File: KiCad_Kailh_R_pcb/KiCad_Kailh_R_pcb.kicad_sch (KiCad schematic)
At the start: 66 parts, among them J1 AudioJack3_SwitchTR, J2 Reset, SW1 Esc, SW10 E, SW11 R, SW12 T, SW13 Ctrl, SW14 A, SW15 S, SW16 D, SW17 F, SW18 G, SW19 Shift, SW2 1, SW20 Z, SW21 X, SW22 C, SW23 V, SW24 6, SW25 Fn, SW26 Alt, SW27 Win, SW28 NoConv, SW29 Space, SW3 2, SW4 3, SW5 4, SW6 5, SW7 Tab, SW8 Q, SW9 W, U1 Sparkfun_Pro_Micro

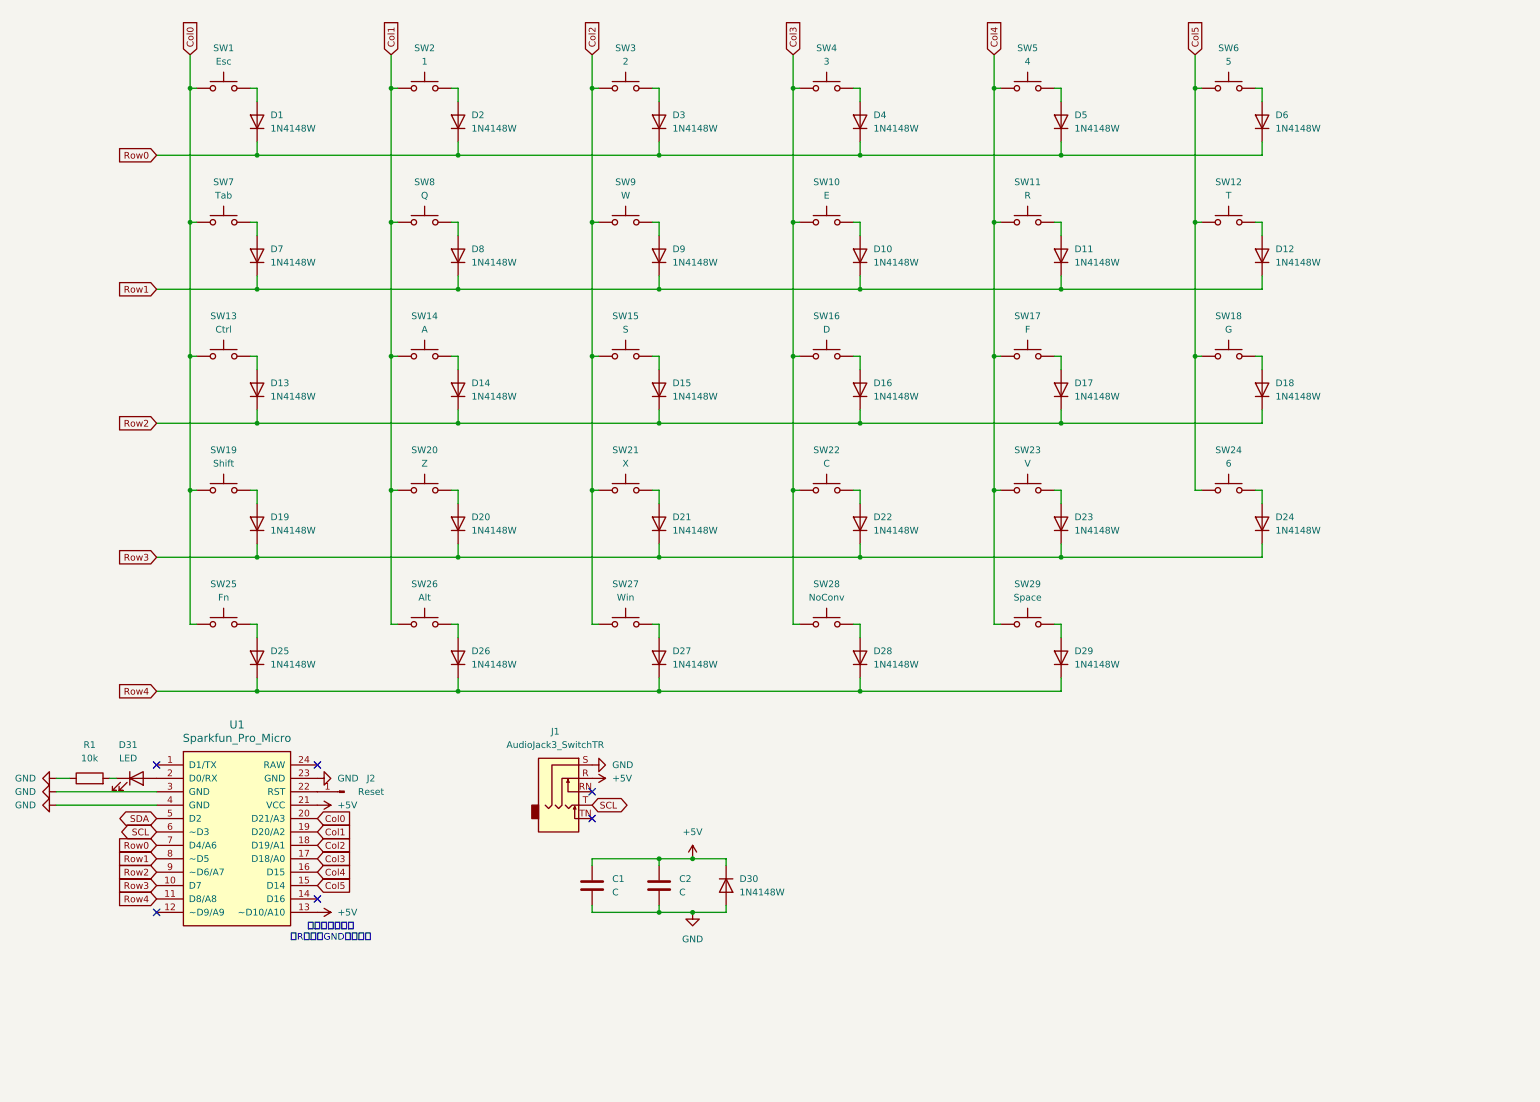
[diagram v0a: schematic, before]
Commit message: feat: Rightのガワを用意
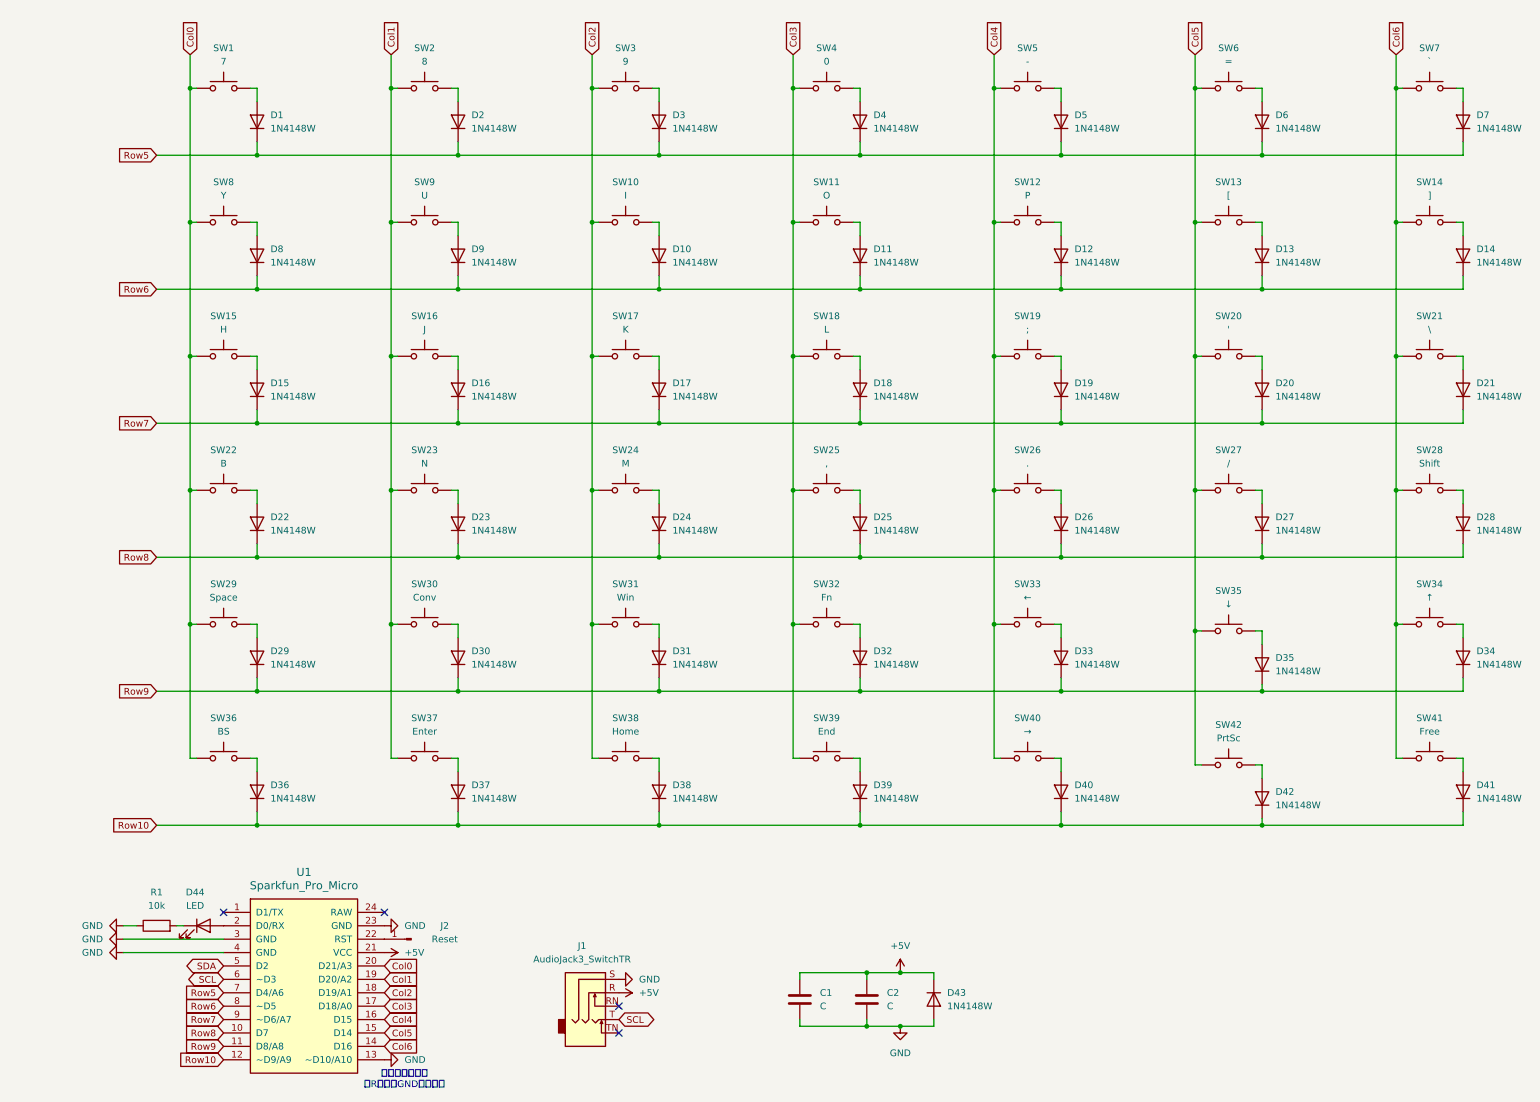
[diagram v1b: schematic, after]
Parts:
- removed D31: LED, LED_SMD:LED_0805_2012Metric, symbol Device:LED
- added D14, D21, D28, D34, D35, D36, D37, D38, D39, D40, D41, D42, D7: 1N4148W, Diode_SMD:D_SOD-323, symbol Diode:1N4148W
- added D44: LED, LED_SMD:LED_0805_2012Metric, symbol Device:LED
- added SW14: ], PCM_Switch_Keyboard_Hotswap_Kailh:SW_Hotswap_Kailh_Choc_V2_1.00u, symbol Switch:SW_Push
- added SW21: \, PCM_Switch_Keyboard_Hotswap_Kailh:SW_Hotswap_Kailh_Choc_V2_1.00u, symbol Switch:SW_Push
- added SW28: Shift, PCM_Switch_Keyboard_Hotswap_Kailh:SW_Hotswap_Kailh_Choc_V2_1.75u, symbol Switch:SW_Push
- added SW34: ↑, PCM_Switch_Keyboard_Hotswap_Kailh:SW_Hotswap_Kailh_Choc_V2_1.00u, symbol Switch:SW_Push
- added SW35: ↓, PCM_Switch_Keyboard_Hotswap_Kailh:SW_Hotswap_Kailh_Choc_V2_1.00u, symbol Switch:SW_Push
- added SW36: BS, PCM_Switch_Keyboard_Hotswap_Kailh:SW_Hotswap_Kailh_Choc_V2_1.00u, symbol Switch:SW_Push
- added SW37: Enter, PCM_Switch_Keyboard_Hotswap_Kailh:SW_Hotswap_Kailh_Choc_V2_ISOEnter, symbol Switch:SW_Push
- added SW38: Home, PCM_Switch_Keyboard_Hotswap_Kailh:SW_Hotswap_Kailh_Choc_V2_1.00u, symbol Switch:SW_Push
- added SW39: End, PCM_Switch_Keyboard_Hotswap_Kailh:SW_Hotswap_Kailh_Choc_V2_1.00u, symbol Switch:SW_Push
- added SW40: →, PCM_Switch_Keyboard_Hotswap_Kailh:SW_Hotswap_Kailh_Choc_V2_1.00u, symbol Switch:SW_Push
- added SW41: Free, PCM_Switch_Keyboard_Hotswap_Kailh:SW_Hotswap_Kailh_Choc_V2_1.00u, symbol Switch:SW_Push
- added SW42: PrtSc, PCM_Switch_Keyboard_Hotswap_Kailh:SW_Hotswap_Kailh_Choc_V2_1.00u, symbol Switch:SW_Push
- added SW7: `, PCM_Switch_Keyboard_Hotswap_Kailh:SW_Hotswap_Kailh_Choc_V2_1.00u, symbol Switch:SW_Push
- SW1: value Esc -> 7; footprint KBD_BrownSugar:CherryMX_Hotswap_via_1U -> PCM_Switch_Keyboard_Hotswap_Kailh:SW_Hotswap_Kailh_Choc_V2_1.00u
- SW10: renamed from SW9; value W -> I; footprint KBD_BrownSugar:CherryMX_Hotswap_via_1U -> PCM_Switch_Keyboard_Hotswap_Kailh:SW_Hotswap_Kailh_Choc_V2_1.00u
- SW11: renamed from SW10; value E -> O; footprint KBD_BrownSugar:CherryMX_Hotswap_via_1U -> PCM_Switch_Keyboard_Hotswap_Kailh:SW_Hotswap_Kailh_Choc_V2_1.00u
- SW12: renamed from SW11; value R -> P; footprint KBD_BrownSugar:CherryMX_Hotswap_via_1U -> PCM_Switch_Keyboard_Hotswap_Kailh:SW_Hotswap_Kailh_Choc_V2_1.00u
- SW13: renamed from SW12; value T -> [; footprint KBD_BrownSugar:CherryMX_Hotswap_via_1U -> PCM_Switch_Keyboard_Hotswap_Kailh:SW_Hotswap_Kailh_Choc_V2_1.00u
- SW15: renamed from SW13; value Ctrl -> H; footprint KBD_BrownSugar:CherryMX_Hotswap_via_1.75U -> PCM_Switch_Keyboard_Hotswap_Kailh:SW_Hotswap_Kailh_Choc_V2_1.00u
- SW16: renamed from SW14; value A -> J; footprint KBD_BrownSugar:CherryMX_Hotswap_via_1U -> PCM_Switch_Keyboard_Hotswap_Kailh:SW_Hotswap_Kailh_Choc_V2_1.00u
- SW17: renamed from SW15; value S -> K; footprint KBD_BrownSugar:CherryMX_Hotswap_via_1U -> PCM_Switch_Keyboard_Hotswap_Kailh:SW_Hotswap_Kailh_Choc_V2_1.00u
- SW18: renamed from SW16; value D -> L; footprint KBD_BrownSugar:CherryMX_Hotswap_via_1U -> PCM_Switch_Keyboard_Hotswap_Kailh:SW_Hotswap_Kailh_Choc_V2_1.00u
- SW19: renamed from SW17; value F -> ;; footprint KBD_BrownSugar:CherryMX_Hotswap_via_1U -> PCM_Switch_Keyboard_Hotswap_Kailh:SW_Hotswap_Kailh_Choc_V2_1.00u
- SW2: value 1 -> 8; footprint KBD_BrownSugar:CherryMX_Hotswap_via_1U -> PCM_Switch_Keyboard_Hotswap_Kailh:SW_Hotswap_Kailh_Choc_V2_1.00u
- SW20: renamed from SW18; value G -> '; footprint KBD_BrownSugar:CherryMX_Hotswap_via_1U -> PCM_Switch_Keyboard_Hotswap_Kailh:SW_Hotswap_Kailh_Choc_V2_1.00u
- SW22: renamed from SW19; value Shift -> B; footprint KBD_BrownSugar:CherryMX_Hotswap_via_2.25U -> PCM_Switch_Keyboard_Hotswap_Kailh:SW_Hotswap_Kailh_Choc_V2_1.00u
- SW23: renamed from SW20; value Z -> N; footprint KBD_BrownSugar:CherryMX_Hotswap_via_1U -> PCM_Switch_Keyboard_Hotswap_Kailh:SW_Hotswap_Kailh_Choc_V2_1.00u
- SW24: renamed from SW21; value X -> M; footprint KBD_BrownSugar:CherryMX_Hotswap_via_1U -> PCM_Switch_Keyboard_Hotswap_Kailh:SW_Hotswap_Kailh_Choc_V2_1.00u
- SW25: renamed from SW22; value C -> ,; footprint KBD_BrownSugar:CherryMX_Hotswap_via_1U -> PCM_Switch_Keyboard_Hotswap_Kailh:SW_Hotswap_Kailh_Choc_V2_1.00u
- SW26: renamed from SW23; value V -> .; footprint KBD_BrownSugar:CherryMX_Hotswap_via_1U -> PCM_Switch_Keyboard_Hotswap_Kailh:SW_Hotswap_Kailh_Choc_V2_1.00u
- SW27: renamed from SW24; value 6 -> /; footprint KBD_BrownSugar:CherryMX_Hotswap_via_1U -> PCM_Switch_Keyboard_Hotswap_Kailh:SW_Hotswap_Kailh_Choc_V2_1.00u
- SW29: renamed from SW25; value Fn -> Space; footprint KBD_BrownSugar:CherryMX_Hotswap_via_1.25U -> PCM_Switch_Keyboard_Hotswap_Kailh:SW_Hotswap_Kailh_Choc_V2_2.00u
- SW3: value 2 -> 9; footprint KBD_BrownSugar:CherryMX_Hotswap_via_1U -> PCM_Switch_Keyboard_Hotswap_Kailh:SW_Hotswap_Kailh_Choc_V2_1.00u
- SW30: renamed from SW26; value Alt -> Conv; footprint KBD_BrownSugar:CherryMX_Hotswap_via_1.25U -> PCM_Switch_Keyboard_Hotswap_Kailh:SW_Hotswap_Kailh_Choc_V2_1.25u
- SW31: renamed from SW27; footprint KBD_BrownSugar:CherryMX_Hotswap_via_1.25U -> PCM_Switch_Keyboard_Hotswap_Kailh:SW_Hotswap_Kailh_Choc_V2_1.25u
- SW32: renamed from SW28; value NoConv -> Fn; footprint KBD_BrownSugar:CherryMX_Hotswap_via_1.25U -> PCM_Switch_Keyboard_Hotswap_Kailh:SW_Hotswap_Kailh_Choc_V2_1.25u
- SW33: renamed from SW29; value Space -> ←; footprint KBD_BrownSugar:CherryMX_Hotswap_via_2U -> PCM_Switch_Keyboard_Hotswap_Kailh:SW_Hotswap_Kailh_Choc_V2_1.00u
- SW4: value 3 -> 0; footprint KBD_BrownSugar:CherryMX_Hotswap_via_1U -> PCM_Switch_Keyboard_Hotswap_Kailh:SW_Hotswap_Kailh_Choc_V2_1.00u
- SW5: value 4 -> -; footprint KBD_BrownSugar:CherryMX_Hotswap_via_1U -> PCM_Switch_Keyboard_Hotswap_Kailh:SW_Hotswap_Kailh_Choc_V2_1.00u
- SW6: value 5 -> =; footprint KBD_BrownSugar:CherryMX_Hotswap_via_1U -> PCM_Switch_Keyboard_Hotswap_Kailh:SW_Hotswap_Kailh_Choc_V2_1.00u
- SW8: renamed from SW7; value Tab -> Y; footprint KBD_BrownSugar:CherryMX_Hotswap_via_1.5U -> PCM_Switch_Keyboard_Hotswap_Kailh:SW_Hotswap_Kailh_Choc_V2_1.00u
- SW9: renamed from SW8; value Q -> U; footprint KBD_BrownSugar:CherryMX_Hotswap_via_1U -> PCM_Switch_Keyboard_Hotswap_Kailh:SW_Hotswap_Kailh_Choc_V2_1.00u
- renumbered D9 to D10, D10 to D11, D11 to D12, D12 to D13, D13 to D15, D14 to D16, D15 to D17, D16 to D18, D17 to D19, D18 to D20, D19 to D22, D20 to D23, D21 to D24, D22 to D25, D23 to D26, D24 to D27, D25 to D29, D26 to D30, D27 to D31, D28 to D32, D29 to D33, D30 to D43, D7 to D8, D8 to D9
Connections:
- net +5V: no longer U1.13 (~D10/A10)
- net Col0: now also SW36.1
- net Col1: now also SW37.1
- net Col2: now also SW38.1
- net Col3: now also SW39.1
- net Col4: now also SW40.1
- net Col5: now also SW35.1, SW42.1
- net GND: now also U1.13 (~D10/A10)
- net at R1.2: now also D44.1 (K)
- net Row10: now reaches U1.12 (~D9/A9)
- net Row10: now also D36.1 (K), D37.1 (K), D38.1 (K), D39.1 (K), D40.1 (K), D41.1 (K), D42.1 (K)
- net Col6: now reaches U1.14 (D16)
- net Col6: now also SW14.1, SW21.1, SW28.1, SW34.1, SW41.1, SW7.1
- net at U1.2 (D0/RX): now also D44.2 (A)
- net Row0 renamed Row5
- net Row5: now also D7.1 (K)
- net Row1 renamed Row6
- net Row6: now also D14.1 (K)
- net Row2 renamed Row7
- net Row7: now also D21.1 (K)
- net Row3 renamed Row8
- net Row8: now also D28.1 (K)
- net Row4 renamed Row9
- net Row9: now also D34.1 (K), D35.1 (K)
- new net: D21.2 (A), SW21.2
- new net: D38.2 (A), SW38.2
- new net: D14.2 (A), SW14.2
- new net: D39.2 (A), SW39.2
- new net: D36.2 (A), SW36.2
- new net: D42.2 (A), SW42.2
- new net: D35.2 (A), SW35.2
- new net: D40.2 (A), SW40.2
- new net: D7.2 (A), SW7.2
- new net: D28.2 (A), SW28.2
- new net: D41.2 (A), SW41.2
- new net: D37.2 (A), SW37.2
- new net: D34.2 (A), SW34.2
- no-connect marks 6 -> 4
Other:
- title: Just the Two of JIS - Left -> Just the Two of JIS - Right
- moved on the sheet: C1, C2, D43, J1, R1, U1
